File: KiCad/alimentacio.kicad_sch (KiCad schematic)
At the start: 0 parts

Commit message: he canviat el micro
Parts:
- added C3: 100uF, symbol Device:C
- added C4: 100u, symbol Device:C
- added D8: SS34, Diode_SMD:D_SMA, symbol Diode:SS34
- added L1: 33uH, symbol Device:L
- added U5: LM2596S-5, Package_TO_SOT_SMD:TO-263-5_TabPin3, symbol Regulator_Switching:LM2596S-5
- added U6: LM1117MP-3.3, Package_TO_SOT_SMD:SOT-223-3_TabPin2, symbol Regulator_Linear:LM1117MP-3.3
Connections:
- new net: D8.2 (A), L1.1, U5.2 (OUT)
- new net 12V: C4.1, U5.1 (VIN)
- new net 3V3: U6.2 (VO)
- new net 5V: C3.1, L1.2, U5.4 (FB), U6.3 (VI)
- new net GND: C3.2, C4.2, D8.1 (K), U5.3 (GND), U5.5 (~{ON}/OFF), U6.1 (GND)
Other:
- note added: "DC-DC"
- note added: "REGULADOR LDO"

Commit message: ERC i footprints
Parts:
- C3: footprint (none) -> Capacitor_SMD:CP_Elec_6.3x5.4
- C4: value 100u -> 100nF; footprint (none) -> Capacitor_SMD:C_0805_2012Metric_Pad1.18x1.45mm_HandSolder
- L1: footprint (none) -> Inductor_SMD:L_7.3x7.3_H4.5

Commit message: routing
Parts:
- added C10, C11: 10uF, Capacitor_SMD:C_0805_2012Metric_Pad1.18x1.45mm_HandSolder, symbol Device:C_Small_US
- added J4: Conn_01x02_Pin, TerminalBlock:TerminalBlock_MaiXu_MX126-5.0-02P_1x02_P5.00mm, symbol Connector:Conn_01x02_Pin
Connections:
- net 12V: now also J4.2 (Pin_2)
- net 3V3: now also C11.1
- net 5V: now also C10.1
- net GND: now also C10.2, C11.2, J4.1 (Pin_1)
- net OUT: now reaches D8.2 (A), L1.1, U5.2 (OUT)

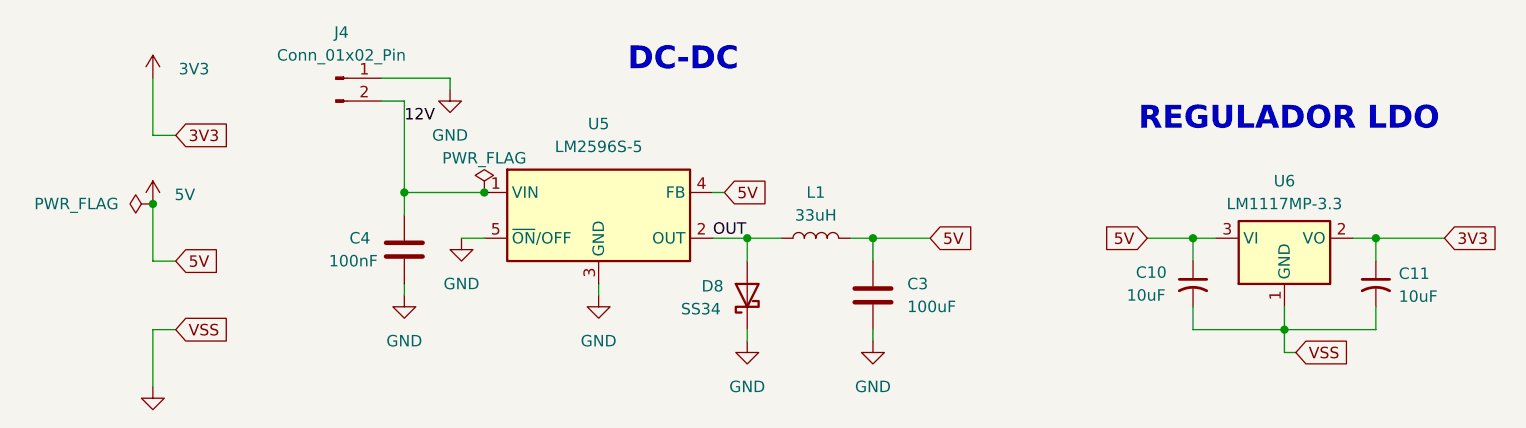
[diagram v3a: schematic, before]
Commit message: correcció d'errors CADLAB, falten els de llums i un parell que no entenc
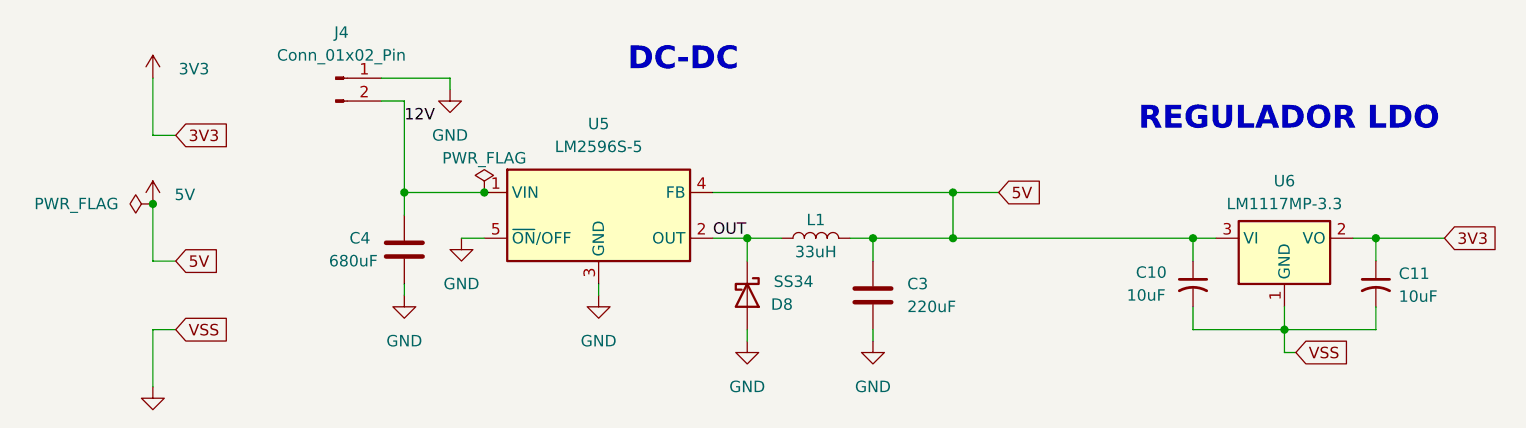
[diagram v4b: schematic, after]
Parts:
- C3: value 100uF -> 220uF
- C4: value 100nF -> 680uF
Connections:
- net GND: now also D8.2 (A); no longer D8.1 (K)
- net OUT: now also D8.1 (K); no longer D8.2 (A)
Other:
- moved on the sheet: D8
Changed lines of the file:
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@@
+	)
+	(junction
+		(at 175.26 101.6)
+		(diameter 0)
+		(color 0 0 0 0)
+	)
+	(junction
+		(at 175.26 96.52)
+		(diameter 0)
+		(color 0 0 0 0)
 	)
 	(junction
@@
 	(wire
 		(pts
-			(xy 196.85 101.6) (xy 201.93 101.6)
-		)
-		(stroke
-			(width 0)
-			(type default)
-		)
-	)
-	(wire
-		(pts
 			(xy 88.9 90.17) (xy 86.36 90.17)
 		)
@@
 	(wire
 		(pts
+			(xy 175.26 101.6) (xy 201.93 101.6)
+		)
+		(stroke
+			(width 0)
+			(type default)
+		)
+	)
+	(wire
+		(pts
+			(xy 175.26 96.52) (xy 180.34 96.52)
+		)
+		(stroke
+			(width 0)
+			(type default)
+		)
+	)
+	(wire
+		(pts
 			(xy 222.25 101.6) (xy 222.25 104.14)
 		)
@@
 	(wire
 		(pts
-			(xy 166.37 101.6) (xy 172.72 101.6)
+			(xy 166.37 101.6) (xy 175.26 101.6)
+		)
+		(stroke
+			(width 0)
+			(type default)
+		)
+	)
+	(wire
+		(pts
+			(xy 175.26 96.52) (xy 175.26 101.6)
 		)
 		(stroke
@@
 	(wire
 		(pts
-			(xy 149.86 96.52) (xy 148.59 96.52)
+			(xy 148.59 96.52) (xy 175.26 96.52)
 		)
 		(stroke
@@
 	(global_label "5V"
 		(shape input)
-		(at 172.72 101.6 0)
+		(at 180.34 96.52 0)
 		(fields_autoplaced yes)
 		(effects
@@
 		)
 		(property "Intersheetrefs" "${INTERSHEET_REFS}"
-			(at 178.0033 101.6 0)
-			(effects
-				(font
-					(size 1.27 1.27)
-				)
-				(justify left)
-				(hide yes)
-			)
-		)
-	)
-	(global_label "5V"
-		(shape input)
-		(at 149.86 96.52 0)
-		(fields_autoplaced yes)
-		(effects
-			(font
-				(size 1.27 1.27)
-			)
-			(justify left)
-		)
-		(property "Intersheetrefs" "${INTERSHEET_REFS}"
-			(at 155.1433 96.52 0)
+			(at 185.6233 96.52 0)
 			(effects
 				(font
@@
 		)
 	)
-	(global_label "5V"
-		(shape input)
-		(at 196.85 101.6 180)
-		(fields_autoplaced yes)
-		(effects
-			(font
-				(size 1.27 1.27)
-			)
-			(justify right)
-		)
-		(property "Intersheetrefs" "${INTERSHEET_REFS}"
-			(at 191.5667 101.6 0)
-			(effects
-				(font
-					(size 1.27 1.27)
-				)
-				(justify right)
-				(hide yes)
-			)
-		)
-	)
 	(symbol
 		(lib_id "Connector:Conn_01x02_Pin")
@@
 		(on_board yes)
 		(dnp no)
-		(fields_autoplaced yes)
 		(property "Reference" "L1"
-			(at 160.02 96.52 90)
+			(at 160.02 99.568 90)
 			(effects
 				(font
@@
 		)
 		(property "Value" "33uH"
-			(at 160.02 99.06 90)
+			(at 160.02 103.124 90)
 			(effects
 				(font
@@
 			)
 		)
-		(property "Value" "100uF"
+		(property "Value" "220uF"
 			(at 170.18 109.2199 0)
 			(effects
@@
 			)
 		)
-		(property "Value" "100nF"
+		(property "Value" "680uF"
 			(at 105.918 104.14 0)
 			(effects
@@
 	(symbol
 		(lib_id "Diode:SS34")
-		(at 152.4 107.95 90)
+		(at 152.4 107.95 270)
 		(unit 1)
 		(exclude_from_sim no)
@@
 		(dnp no)
 		(property "Reference" "D8"
-			(at 147.32 106.934 90)
+			(at 157.48 108.966 90)
 			(effects
 				(font
@@
 		)
 		(property "Value" "SS34"
-			(at 145.034 109.474 90)
+			(at 159.766 106.426 90)
 			(effects
 				(font
@@
 		)
 		(property "Footprint" "Diode_SMD:D_SMA"
-			(at 156.845 107.95 0)
-			(effects
-				(font
+			(at 147.955 107.95 0)
+			(effects
+				(font

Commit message: alguns errors de CADLAB i he canivat d'ordre els LEDs i els drivers a la PCB.
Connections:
- net 12V: now also J4.1 (Pin_1); no longer J4.2 (Pin_2)
- net GND: now also J4.2 (Pin_2); no longer C10.2, C11.2, J4.1 (Pin_1), U6.1 (GND)
- net 3V3 renamed +3V3
- net 5V renamed +5V
- new net VSS: C10.2, C11.2, U6.1 (GND)
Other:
- moved on the sheet: J4

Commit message: modificacions cadlab
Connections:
- net VSS is gone; now on net GND: C10.2, C11.2, U6.1 (GND)
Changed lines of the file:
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@@
+	(wire
+		(pts
+			(xy 166.37 101.6) (xy 163.83 101.6)
+		)
+		(stroke
+			(width 0)
+			(type default)
+		)
+	)
+	(wire
+		(pts
+			(xy 201.93 101.6) (xy 204.47 101.6)
+		)
+		(stroke
+			(width 0)
+			(type default)
+		)
+	)
+	(wire
+		(pts
+			(xy 135.89 107.95) (xy 135.89 106.68)
+		)
+		(stroke
+			(width 0)
+			(type default)
+		)
+	)
+	(wire
+		(pts
+			(xy 114.3 107.95) (xy 114.3 106.68)
+		)
+		(stroke
+			(width 0)
+			(type default)
+		)
+	)
+	(wire
+		(pts
+			(xy 222.25 101.6) (xy 231.14 101.6)
+		)
+		(stroke
+			(width 0)
+			(type default)
+		)
+	)
+	(wire
+		(pts
+			(xy 180.34 93.98) (xy 180.34 96.52)
+		)
+		(stroke
+			(width 0)
+			(type default)
+		)
+	)
+	(wire
+		(pts
+			(xy 201.93 109.22) (xy 201.93 111.76)
+		)
+		(stroke
+			(width 0)
+			(type default)
+		)
+	)
+	(wire
+		(pts
+			(xy 109.22 88.9) (xy 102.87 88.9)
+		)
+		(stroke
+			(width 0)
+			(type default)
+		)
+	)
+	(wire
+		(pts
+			(xy 222.25 109.22) (xy 222.25 111.76)
+		)
+		(stroke
+			(width 0)
+			(type default)
+		)
+	)
+	(wire
+		(pts
+			(xy 114.3 86.36) (xy 102.87 86.36)
+		)
+		(stroke
+			(width 0)
+			(type default)
+		)
+	)
+	(wire
+		(pts
+			(xy 201.93 101.6) (xy 201.93 104.14)
+		)
+		(stroke
+			(width 0)
+			(type default)
+		)
+	)
+	(wire
+		(pts
+			(xy 152.4 104.14) (xy 152.4 101.6)
+		)
+		(stroke
+			(width 0)
+			(type default)
+		)
+	)
+	(wire
+		(pts
+			(xy 166.37 101.6) (xy 166.37 104.14)
+		)
+		(stroke
+			(width 0)
+			(type default)
+		)
+	)
+	(wire
+		(pts
+			(xy 114.3 96.52) (xy 120.65 96.52)
+		)
+		(stroke
+			(width 0)
+			(type default)
+		)
+	)
+	(wire
+		(pts
+			(xy 148.59 101.6) (xy 152.4 101.6)
+		)
+		(stroke
+			(width 0)
+			(type default)
+		)
+	)
+	(wire
+		(pts
+			(xy 212.09 111.76) (xy 222.25 111.76)
+		)
+		(stroke
+			(width 0)
+			(type default)
+		)
+	)
+	(wire
+		(pts
+			(xy 166.37 111.76) (xy 166.37 113.03)
+		)
+		(stroke
+			(width 0)
+			(type default)
+		)
+	)
+	(wire
+		(pts
+			(xy 212.09 111.76) (xy 212.09 114.3)
+		)
+		(stroke
+			(width 0)
+			(type default)
+		)
+	)
+	(wire
+		(pts
+			(xy 109.22 90.17) (xy 109.22 88.9)
+		)
+		(stroke
+			(width 0)
+			(type default)
+		)
+	)
+	(wire
+		(pts
+			(xy 120.65 96.52) (xy 123.19 96.52)
+		)
+		(stroke
+			(width 0)
+			(type default)
+		)
+	)
 	(wire
 		(pts
@@
 	(wire
 		(pts
-			(xy 166.37 101.6) (xy 163.83 101.6)
-		)
-		(stroke
-			(width 0)
-			(type default)
-		)
-	)
-	(wire
-		(pts
-			(xy 201.93 101.6) (xy 204.47 101.6)
-		)
-		(stroke
-			(width 0)
-			(type default)
-		)
-	)
-	(wire
-		(pts
-			(xy 135.89 107.95) (xy 135.89 106.68)
-		)
-		(stroke
-			(width 0)
-			(type default)
-		)
-	)
-	(wire
-		(pts
-			(xy 114.3 107.95) (xy 114.3 106.68)
-		)
-		(stroke
-			(width 0)
-			(type default)
-		)
-	)
-	(wire
-		(pts
-			(xy 222.25 101.6) (xy 231.14 101.6)
-		)
-		(stroke
-			(width 0)
-			(type default)
-		)
-	)
-	(wire
-		(pts
-			(xy 180.34 93.98) (xy 180.34 96.52)
-		)
-		(stroke
-			(width 0)
-			(type default)
-		)
-	)
-	(wire
-		(pts
-			(xy 201.93 109.22) (xy 201.93 111.76)
-		)
-		(stroke
-			(width 0)
-			(type default)
-		)
-	)
-	(wire
-		(pts
-			(xy 109.22 88.9) (xy 102.87 88.9)
-		)
-		(stroke
-			(width 0)
-			(type default)
-		)
-	)
-	(wire
-		(pts
-			(xy 222.25 109.22) (xy 222.25 111.76)
-		)
-		(stroke
-			(width 0)
-			(type default)
-		)
-	)
-	(wire
-		(pts
-			(xy 114.3 86.36) (xy 102.87 86.36)
-		)
-		(stroke
-			(width 0)
-			(type default)
-		)
-	)
-	(wire
-		(pts
-			(xy 201.93 101.6) (xy 201.93 104.14)
-		)
-		(stroke
-			(width 0)
-			(type default)
-		)
-	)
-	(wire
-		(pts
-			(xy 152.4 104.14) (xy 152.4 101.6)
-		)
-		(stroke
-			(width 0)
-			(type default)
-		)
-	)
-	(wire
-		(pts
-			(xy 166.37 101.6) (xy 166.37 104.14)
-		)
-		(stroke
-			(width 0)
-			(type default)
-		)
-	)
-	(wire
-		(pts
-			(xy 114.3 96.52) (xy 120.65 96.52)
-		)
-		(stroke
-			(width 0)
-			(type default)
-		)
-	)
-	(wire
-		(pts
-			(xy 148.59 101.6) (xy 152.4 101.6)
-		)
-		(stroke
-			(width 0)
-			(type default)
-		)
-	)
-	(wire
-		(pts
-			(xy 212.09 111.76) (xy 222.25 111.76)
-		)
-		(stroke
-			(width 0)
-			(type default)
-		)
-	)
-	(wire
-		(pts
-			(xy 166.37 111.76) (xy 166.37 113.03)
-		)
-		(stroke
-			(width 0)
-			(type default)
-		)
-	)
-	(wire
-		(pts
-			(xy 212.09 111.76) (xy 212.09 114.3)
-		)
-		(stroke
-			(width 0)
-			(type default)
-		)
-	)
-	(wire
-		(pts
-			(xy 109.22 90.17) (xy 109.22 88.9)
-		)
-		(stroke
-			(width 0)
-			(type default)
-		)
-	)
-	(wire
-		(pts
-			(xy 120.65 96.52) (xy 123.19 96.52)
-		)
-		(stroke
-			(width 0)
-			(type default)
-		)
-	)
-	(wire
-		(pts
 			(xy 152.4 113.03) (xy 152.4 111.76)
 		)
@@
 		(pts
 			(xy 148.59 96.52) (xy 175.26 96.52)
-		)
-		(stroke
-			(width 0)
-			(type default)
-		)
-	)
-	(wire
-		(pts
-			(xy 212.09 114.3) (xy 213.36 114.3)
 		)
 		(stroke
@@
 		)
 	)
-	(global_label "VSS"
-		(shape input)
-		(at 213.36 114.3 0)
-		(fields_autoplaced yes)
-		(effects
-			(font
-				(size 1.27 1.27)
-			)
-			(justify left)
-		)
-		(property "Intersheetrefs" "${INTERSHEET_REFS}"
-			(at 219.8528 114.3 0)
-			(effects
-				(font
-					(size 1.27 1.27)
-				)
-				(justify left)
-				(hide yes)
-			)
-		)
-	)
 	(symbol
 		(lib_id "Connector:Conn_01x02_Pin")
@@
 					(unit 1)
 				)
+			)
+		)
+	)
+	(symbol
+		(lib_id "power:GND")
+		(at 212.09 114.3 0)
+		(unit 1)
+		(exclude_from_sim no)
+		(in_bom yes)
+		(on_board yes)
+		(dnp no)
+		(fields_autoplaced yes)
+		(property "Reference" "#PWR052"
+			(at 212.09 120.65 0)
+			(effects
+				(font
+					(size 1.27 1.27)
+				)
+				(hide yes)
+			)
+		)
+		(property "Value" "GND"
+			(at 212.09 119.38 0)
+			(effects
+				(font
+					(size 1.27 1.27)
+				)
+			)
+		)
+		(property "Footprint" ""
+			(at 212.09 114.3 0)
+			(effects
+				(font
+					(size 1.27 1.27)
+				)
+				(hide yes)
+			)
+		)
+		(property "Datasheet" ""
+			(at 212.09 114.3 0)
+			(effects
+				(font
+					(size 1.27 1.27)
+				)
+				(hide yes)
+			)
+		)
+		(property "Description" "Power symbol creates a global label with name \"GND\" , ground"
+			(at 212.09 114.3 0)
+			(effects
+				(font
+					(size 1.27 1.27)
+				)
+				(hide yes)
+			)
+		)
+		(pin "1"
+		)
+		(instances
+			(project "PROJECTE_LLUMS"
+				(path "/b4874c87-978f-427f-bc45-3635f8629977/b442c7ef-ea3d-476f-b4ca-53d1479b8362"
+					(reference "#PWR052")
+					(unit 1)
+				)

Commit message: coses
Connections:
- net GND: no longer C3.2, C4.2, D8.2 (A), J4.2 (Pin_2), U5.3 (GND), U5.5 (~{ON}/OFF)
- new net GNDPWR: C3.2, C4.2, D8.2 (A), J4.2 (Pin_2), U5.3 (GND), U5.5 (~{ON}/OFF)

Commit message: test points schematic
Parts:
- added D1: LED, LED_SMD:LED_0805_2012Metric_Pad1.15x1.40mm_HandSolder, symbol Device:LED
- added R2: 680, Resistor_SMD:R_0805_2012Metric_Pad1.20x1.40mm_HandSolder, symbol Device:R
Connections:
- net +5V: now also R2.1
- net GND: now also D1.1 (K)
- new net: D1.2 (A), R2.2
